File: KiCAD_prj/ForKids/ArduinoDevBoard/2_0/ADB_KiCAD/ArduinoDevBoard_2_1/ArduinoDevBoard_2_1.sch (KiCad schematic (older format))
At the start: 43 parts, among them J1 LCD1602, J10 +5V, J11 GND, J12 Buzzer, J13 Bluetooth, J14 M-PWM, J15 Servo SG90, J16 Conn_01x02_Female, J17 Conn_01x02_Female, J18 Conn_01x02_Female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

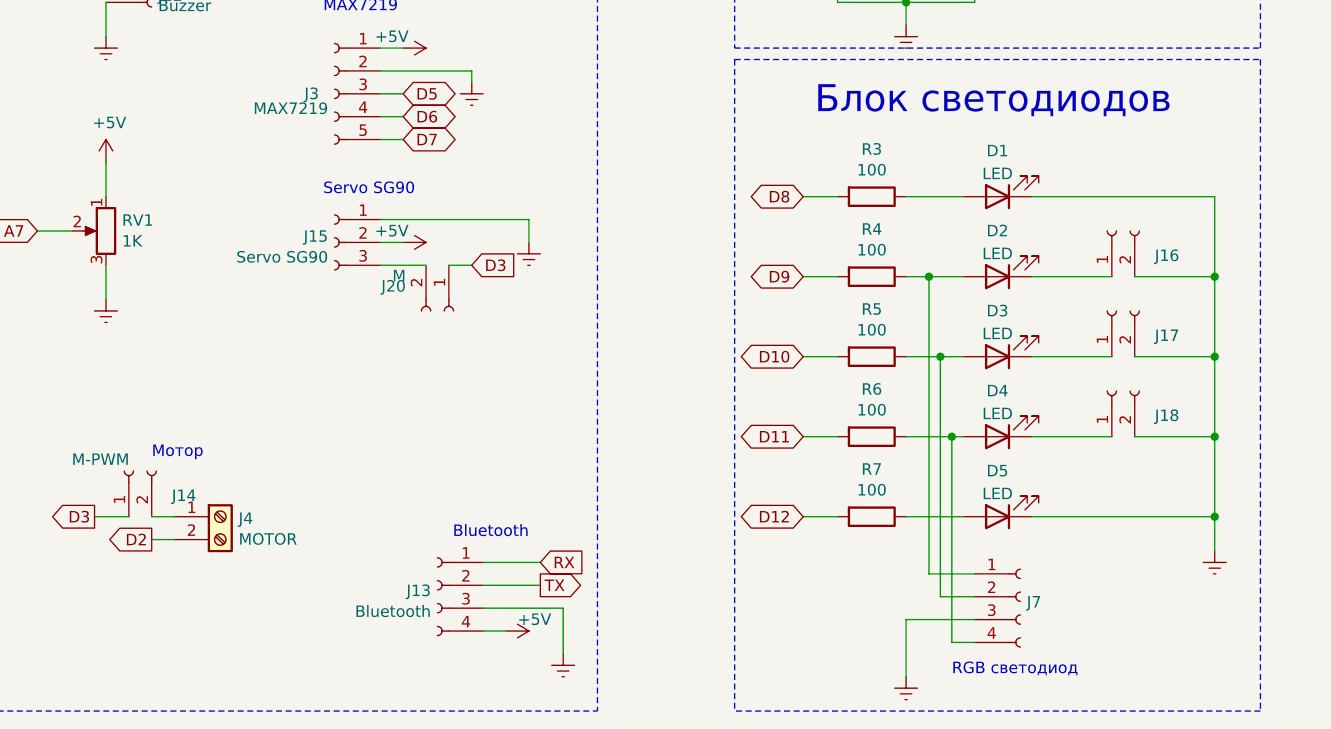
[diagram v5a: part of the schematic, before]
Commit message: Update ADB 2.1 end NanoMotors projects
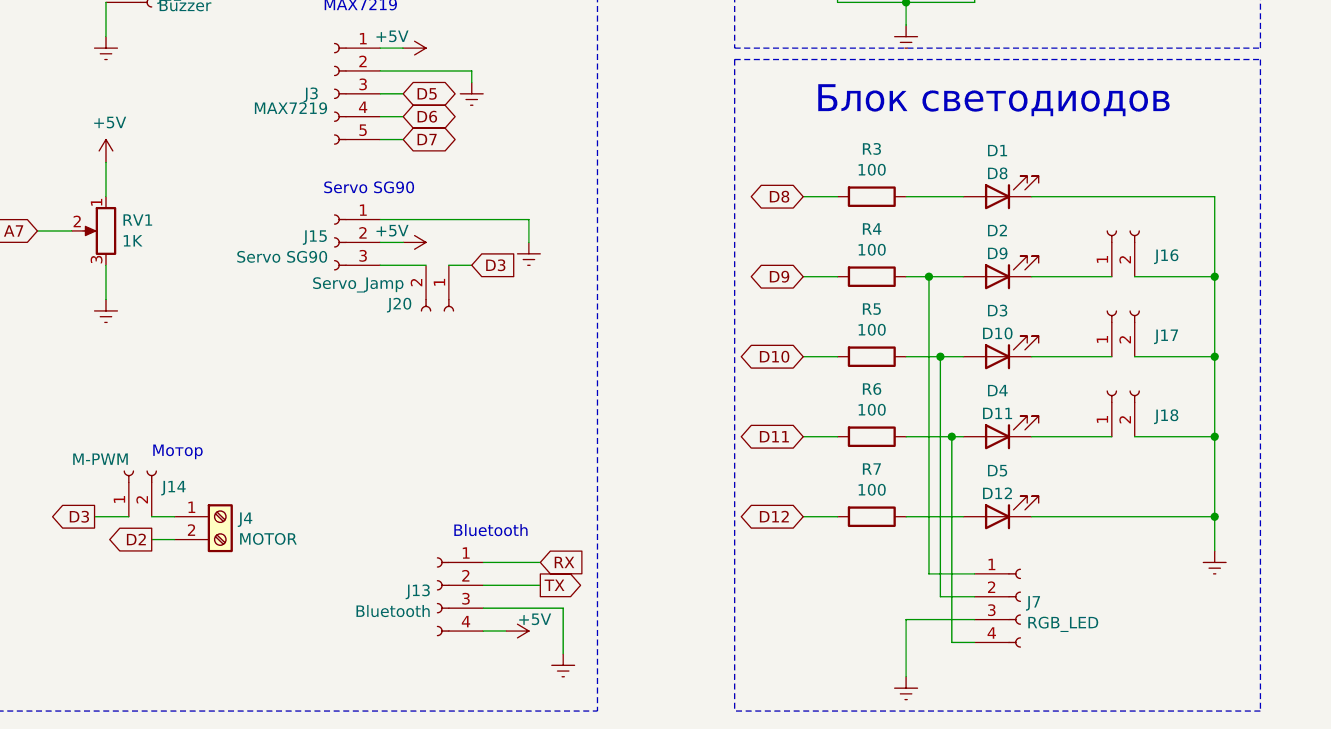
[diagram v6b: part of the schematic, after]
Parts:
- D1: value LED -> D8
- D2: value LED -> D9
- D3: value LED -> D10
- D4: value LED -> D11
- D5: value LED -> D12
- J16: value Conn_01x02_Female -> D9
- J17: value Conn_01x02_Female -> D10
- J18: value Conn_01x02_Female -> D11
- J20: value M -> Servo_Jamp
- J5: value Conn_01x02_Female -> VIN_JAMP_1
- J6: value Conn_01x02_Female -> VIN_JAMP_2
- J7: value Conn_01x04_Female -> RGB_LED
- SW1: value SW_Push_Dual -> D13
- SW2: value SW_Push_Dual -> D16
- SW3: value SW_Push_Dual -> D17
- U1: footprint Package_TO_SOT_THT:TO-92_Wide -> Package_TO_SOT_SMD:TO-252-3_TabPin2
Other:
- note removed: "RGB светодиод"
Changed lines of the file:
@@
 F 0 "U1" H 2250 1600 50  0000 C CNN
 F 1 "LM78M05_TO220" H 2250 1750 50  0000 C CNN
-F 2 "Package_TO_SOT_THT:TO-92_Wide" H 2250 1825 50  0001 C CIN
+F 2 "Package_TO_SOT_SMD:TO-252-3_TabPin2" H 2250 1825 50  0001 C CIN
 F 3 "http://www.fairchildsemi.com/ds/LM/LM78M05.pdf" H 2250 1550 50  0001 C CNN
 	1    2250 1600
@@
 P 2700 1400
 F 0 "J6" V 2592 1212 50  0000 R CNN
-F 1 "Conn_01x02_Female" V 2547 1212 50  0001 R CNN
+F 1 "VIN_JAMP_2" V 2547 1212 50  0001 R CNN
 F 2 "Connector_PinHeader_2.54mm:PinHeader_1x02_P2.54mm_Vertical" H 2700 1400 50  0001 C CNN
 F 3 "~" H 2700 1400 50  0001 C CNN
@@
 P 1700 1400
 F 0 "J5" V 1600 1550 50  0000 R CNN
-F 1 "Conn_01x02_Female" V 1547 1212 50  0001 R CNN
+F 1 "VIN_JAMP_1" V 1547 1212 50  0001 R CNN
 F 2 "Connector_PinHeader_2.54mm:PinHeader_1x02_P2.54mm_Vertical" H 1700 1400 50  0001 C CNN
 F 3 "~" H 1700 1400 50  0001 C CNN
@@
 P 5500 5350
 F 0 "D1" H 5500 5150 50  0000 C CNN
-F 1 "LED" H 5500 5250 50  0000 C CNN
+F 1 "D8" H 5500 5250 50  0000 C CNN
 F 2 "LED_THT:LED_D5.0mm" H 5500 5350 50  0001 C CNN
 F 3 "~" H 5500 5350 50  0001 C CNN
@@
 P 5500 5700
 F 0 "D2" H 5500 5500 50  0000 C CNN
-F 1 "LED" H 5500 5600 50  0000 C CNN
+F 1 "D9" H 5500 5600 50  0000 C CNN
 F 2 "LED_THT:LED_D5.0mm" H 5500 5700 50  0001 C CNN
 F 3 "~" H 5500 5700 50  0001 C CNN
@@
 P 5500 6050
 F 0 "D3" H 5500 5850 50  0000 C CNN
-F 1 "LED" H 5500 5950 50  0000 C CNN
+F 1 "D10" H 5500 5950 50  0000 C CNN
 F 2 "LED_THT:LED_D5.0mm" H 5500 6050 50  0001 C CNN
 F 3 "~" H 5500 6050 50  0001 C CNN
@@
 P 5500 6400
 F 0 "D4" H 5500 6200 50  0000 C CNN
-F 1 "LED" H 5500 6300 50  0000 C CNN
+F 1 "D11" H 5500 6300 50  0000 C CNN
 F 2 "LED_THT:LED_D5.0mm" H 5500 6400 50  0001 C CNN
 F 3 "~" H 5500 6400 50  0001 C CNN
@@
 P 5500 6750
 F 0 "D5" H 5500 6550 50  0000 C CNN
-F 1 "LED" H 5500 6650 50  0000 C CNN
+F 1 "D12" H 5500 6650 50  0000 C CNN
 F 2 "LED_THT:LED_D5.0mm" H 5500 6750 50  0001 C CNN
 F 3 "~" H 5500 6750 50  0001 C CNN
@@
 P 5600 7100
 F 0 "J7" H 5628 7076 50  0000 L CNN
-F 1 "Conn_01x04_Female" H 5628 6985 50  0001 L CNN
+F 1 "RGB_LED" H 5628 6985 50  0000 L CNN
 F 2 "Connector_PinHeader_2.54mm:PinHeader_1x04_P2.54mm_Vertical" H 5600 7100 50  0001 C CNN
 F 3 "~" H 5600 7100 50  0001 C CNN
@@
 Wire Wire Line
 	5100 5700 5200 5700
-Text Notes 5300 7450 0    50   ~ 0
-RGB светодиод
 Wire Wire Line
 	5100 6050 5250 6050
@@
 P 6000 5500
 F 0 "J16" V 5892 5312 50  0000 R CNN
-F 1 "Conn_01x02_Female" V 5847 5312 50  0001 R CNN
+F 1 "D9" V 5847 5312 50  0001 R CNN
 F 2 "Connector_PinHeader_2.54mm:PinHeader_1x02_P2.54mm_Vertical" H 6000 5500 50  0001 C CNN
 F 3 "~" H 6000 5500 50  0001 C CNN
@@
 P 6000 5850
 F 0 "J17" V 5892 5662 50  0000 R CNN
-F 1 "Conn_01x02_Female" V 5847 5662 50  0001 R CNN
+F 1 "D10" V 5847 5662 50  0001 R CNN
 F 2 "Connector_PinHeader_2.54mm:PinHeader_1x02_P2.54mm_Vertical" H 6000 5850 50  0001 C CNN
 F 3 "~" H 6000 5850 50  0001 C CNN
@@
 P 6000 6200
 F 0 "J18" V 5892 6012 50  0000 R CNN
-F 1 "Conn_01x02_Female" V 5847 6012 50  0001 R CNN
+F 1 "D11" V 5847 6012 50  0001 R CNN
 F 2 "Connector_PinHeader_2.54mm:PinHeader_1x02_P2.54mm_Vertical" H 6000 6200 50  0001 C CNN
 F 3 "~" H 6000 6200 50  0001 C CNN
@@
 U 1 1 5FF97A28
 P 3100 5850
-F 0 "J20" V 2992 5662 50  0000 R CNN
-F 1 "M" V 2947 5662 50  0000 R CNN
+F 0 "J20" V 3070 5690 50  0000 R CNN
+F 1 "Servo_Jamp" V 2980 5655 50  0000 R CNN
 F 2 "Connector_PinHeader_2.54mm:PinHeader_1x02_P2.54mm_Vertical" H 3100 5850 50  0001 C CNN
 F 3 "~" H 3100 5850 50  0001 C CNN
@@
 U 1 1 601C1F03
 P 1700 6550
-F 0 "J14" V 1592 6362 50  0000 R CNN
+F 0 "J14" V 1630 6405 50  0000 R CNN
 F 1 "M-PWM" V 1750 6800 50  0000 R CNN
 F 2 "Connector_PinHeader_2.54mm:PinHeader_1x02_P2.54mm_Vertical" H 1700 6550 50  0001 C CNN
@@
 P 5850 2950
 F 0 "SW1" H 5550 3050 50  0000 C CNN
-F 1 "SW_Push_Dual" H 5850 3144 50  0001 C CNN
+F 1 "D13" H 5850 3144 50  0001 C CNN
 F 2 "Button_Switch_THT:SW_PUSH_6mm" H 5850 3150 50  0001 C CNN
 F 3 "~" H 5850 3150 50  0001 C CNN
@@
 P 5850 3300
 F 0 "SW2" H 5550 3400 50  0000 C CNN
-F 1 "SW_Push_Dual" H 5850 3494 50  0001 C CNN
+F 1 "D16" H 5850 3494 50  0001 C CNN
 F 2 "Button_Switch_THT:SW_PUSH_6mm" H 5850 3500 50  0001 C CNN
 F 3 "~" H 5850 3500 50  0001 C CNN
@@
 P 5850 3650
 F 0 "SW3" H 5550 3750 50  0000 C CNN
-F 1 "SW_Push_Dual" H 5850 3844 50  0001 C CNN
+F 1 "D17" H 5850 3844 50  0001 C CNN
 F 2 "Button_Switch_THT:SW_PUSH_6mm" H 5850 3850 50  0001 C CNN
 F 3 "~" H 5850 3850 50  0001 C CNN

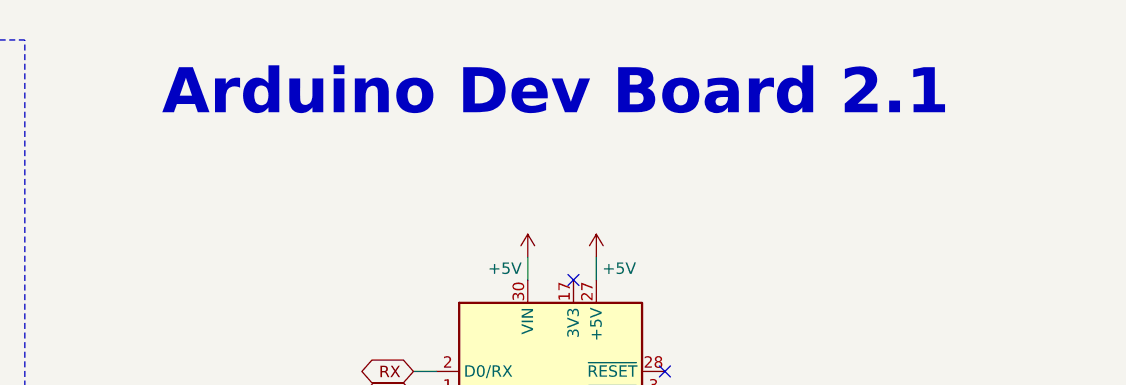
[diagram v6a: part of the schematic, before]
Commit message: Update ArduinoDevBoard 2: ad .pdf file. Rename title to schem
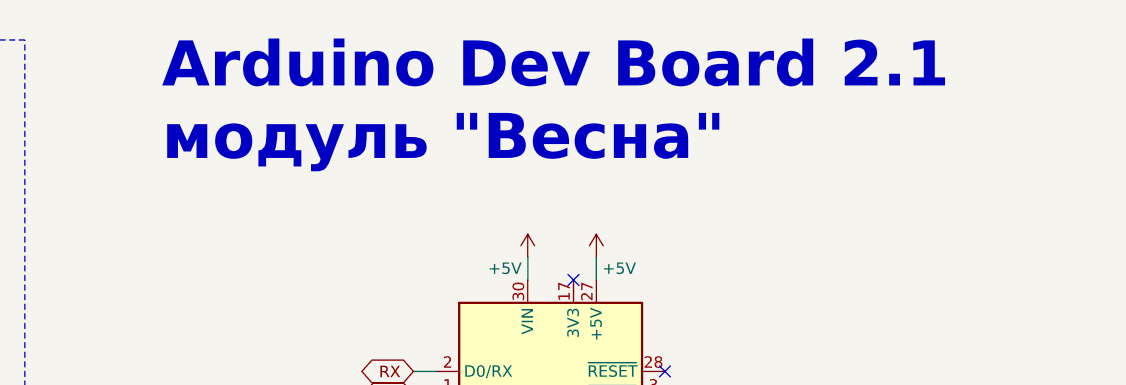
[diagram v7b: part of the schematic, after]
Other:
- note added: "Arduino Dev Board 2.1\nмодуль "Весна""
- note removed: "Arduino Dev Board 2.1"
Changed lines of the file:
@@
 	1    0    0    -1
 $EndComp
-Text Notes 7250 1050 0    197  ~ 39
-Arduino Dev Board 2.1
 Wire Wire Line
 	5100 5700 5200 5700
@@
 NoConn ~ 5650 3850
 NoConn ~ 9050 1750
+Text Notes 7250 1250 0    197  ~ 39
+Arduino Dev Board 2.1\nмодуль "Весна"
 $EndSCHEMATC

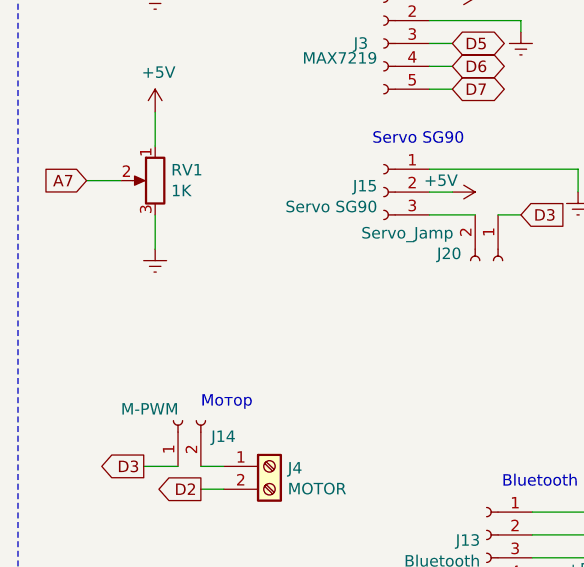
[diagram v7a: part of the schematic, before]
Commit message: Fix ArduinoDevBoard 2.0 project: add resistor 100 R to knob
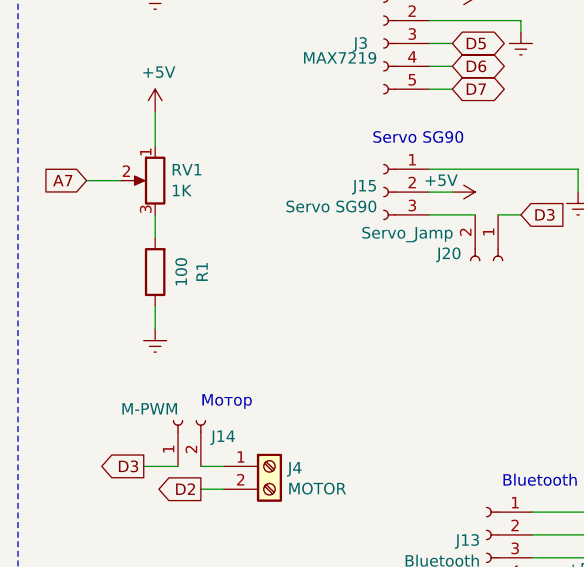
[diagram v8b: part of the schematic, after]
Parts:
- added R1: 100, Resistor_THT:R_Axial_DIN0411_L9.9mm_D3.6mm_P12.70mm_Horizontal, symbol Device:R
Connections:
- net Earth: now also R1.1; no longer RV1.3
- new net: R1.2, RV1.3
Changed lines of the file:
@@
 L power:Earth #PWR028
 U 1 1 5E041882
-P 1600 5800
-F 0 "#PWR028" H 1600 5550 50  0001 C CNN
-F 1 "Earth" H 1600 5650 50  0001 C CNN
-F 2 "" H 1600 5800 50  0001 C CNN
-F 3 "~" H 1600 5800 50  0001 C CNN
-	1    1600 5800
-	1    0    0    -1
-$EndComp
-Wire Wire Line
-	1600 5800 1600 5650
+P 1600 6150
+F 0 "#PWR028" H 1600 5900 50  0001 C CNN
+F 1 "Earth" H 1600 6000 50  0001 C CNN
+F 2 "" H 1600 6150 50  0001 C CNN
+F 3 "~" H 1600 6150 50  0001 C CNN
+	1    1600 6150
+	1    0    0    -1
+$EndComp
 $Comp
 L power:+5V #PWR027
@@
 Text Notes 7250 1250 0    197  ~ 39
 Arduino Dev Board 2.1\nмодуль "Весна"
+$Comp
+L Device:R R1
+U 1 1 60409FB0
+P 1600 5900
+F 0 "R1" V 1393 5900 50  0000 C CNN
+F 1 "100" V 1484 5900 50  0000 C CNN
+F 2 "Resistor_THT:R_Axial_DIN0411_L9.9mm_D3.6mm_P12.70mm_Horizontal" V 1530 5900 50  0001 C CNN
+F 3 "~" H 1600 5900 50  0001 C CNN
+	1    1600 5900
+	-1   0    0    1
+$EndComp
+Wire Wire Line
+	1600 5650 1600 5750
+Wire Wire Line
+	1600 6050 1600 6150
 $EndSCHEMATC
